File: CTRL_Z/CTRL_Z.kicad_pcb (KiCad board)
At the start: 2 copper layers, 25 x 20 mm, 6 parts, among them J1 BM04B-NSHSS-TBT_LF__SN_

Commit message: CTRL Z, R, PWR Cleanup! Changes Made:
CTRL PWR -> Added Ground Plane and Ground Vias. Moved it out of parent folder CTRL_R upto Root.
CTRL Z ->  Removed Unnecessary ZX pin. Added Ground Plane and Ground Vias.
CTRL R -> Cleaned up pin count, from 14 down to 10. Added Ground Plane and Ground Vias. Made some modifications to the board shape.
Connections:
- J1 pad 2: Row1_X -> unconnected-(J1-Pad2)
- J1 pad 3: Row1_ZX -> Net-(S1-COM_1)
- S1 pad 1: Row1_X -> Net-(S1-COM_1)
- S1 pad 2: Row1_X -> Net-(S1-COM_1)
- S2 pad 1: Row1_ZX -> Net-(S1-COM_1)
- S2 pad 2: Row1_ZX -> Net-(S1-COM_1)
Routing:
- net Net-(S1-COM_1): track 0.00 -> 33.5 mm, vias 0 -> 1
- net Row1_X: track 16.4 -> 0.00 mm, vias 1 -> 0
- net Row1_ZX: track 14.9 -> 0.00 mm, vias 1 -> 0
- net GND: vias 0 -> 4
- added copper zone on B.Cu, net GND
- added copper zone on F.Cu, net GND
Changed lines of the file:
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@@
 		(sheetname "/")
 		(sheetfile "CTRL_Z.kicad_sch")
+		(units
+			(unit
+				(name "A")
+				(pins)
+			)
+		)
 		(attr exclude_from_bom)
 		(duplicate_pad_numbers_are_jumpers no)
@@
 		(sheetname "/")
 		(sheetfile "CTRL_Z.kicad_sch")
+		(units
+			(unit
+				(name "A")
+				(pins "4" "2" "3" "1")
+			)
+		)
 		(attr smd)
 		(duplicate_pad_numbers_are_jumpers no)
@@
 			(size 1.3 1.55)
 			(layers "F.Cu" "F.Mask" "F.Paste")
-			(net "Row1_ZX")
+			(net "Net-(S1-COM_1)")
 			(pinfunction "COM_1_1")
 			(pintype "passive")
@@
 			(size 1.3 1.55)
 			(layers "F.Cu" "F.Mask" "F.Paste")
-			(net "Row1_ZX")
+			(net "Net-(S1-COM_1)")
 			(pinfunction "COM_2_2")
 			(pintype "passive")
@@
 		(sheetname "/")
 		(sheetfile "CTRL_Z.kicad_sch")
+		(units
+			(unit
+				(name "A")
+				(pins "4" "2" "3" "1")
+			)
+		)
 		(attr smd)
 		(duplicate_pad_numbers_are_jumpers no)
@@
 			(size 1.3 1.55)
 			(layers "F.Cu" "F.Mask" "F.Paste")
-			(net "Row1_X")
+			(net "Net-(S1-COM_1)")
 			(pinfunction "COM_1_1")
 			(pintype "passive")
@@
 			(size 1.3 1.55)
 			(layers "F.Cu" "F.Mask" "F.Paste")
-			(net "Row1_X")
+			(net "Net-(S1-COM_1)")
 			(pinfunction "COM_2_2")
 			(pintype "passive")
@@
 		(sheetname "/")
 		(sheetfile "CTRL_Z.kicad_sch")
+		(units
+			(unit
+				(name "A")
+				(pins)
+			)
+		)
 		(attr exclude_from_bom)
 		(duplicate_pad_numbers_are_jumpers no)
@@
 		(sheetname "/")
 		(sheetfile "CTRL_Z.kicad_sch")
+		(units
+			(unit
+				(name "A")
+				(pins)
+			)
+		)
 		(attr exclude_from_bom)
 		(duplicate_pad_numbers_are_jumpers no)
@@
 		(sheetname "/")
 		(sheetfile "CTRL_Z.kicad_sch")
+		(units
+			(unit
+				(name "A")
+				(pins "6" "5" "4" "3" "2" "1")
+			)
+		)
 		(attr smd)
 		(duplicate_pad_numbers_are_jumpers no)
@@
 			(size 0.6 1.7)
 			(layers "B.Cu" "B.Mask" "B.Paste")
-			(net "Row1_X")
+			(net "unconnected-(J1-Pad2)")
 			(pinfunction "2_2")
-			(pintype "passive")
+			(pintype "passive+no_connect")
 		)
 		(pad "3" smd rect
@@
 			(size 0.6 1.7)
 			(layers "B.Cu" "B.Mask" "B.Paste")
-			(net "Row1_ZX")
+			(net "Net-(S1-COM_1)")
 			(pinfunction "3_3")
 			(pintype "passive")
@@
 	)
 	(segment
-		(start 83.679 114.852)
-		(end 88.879 114.852)
-		(width 0.2)
-		(layer "B.Cu")
-		(net "GND")
+		(start 90.14 112.932)
+		(end 90.14 115.281)
+		(width 0.2)
+		(layer "F.Cu")
+		(net "Net-(S1-COM_1)")
+	)
+	(segment
+		(start 90.165 112.907)
+		(end 90.14 112.932)
+		(width 0.2)
+		(layer "F.Cu")
+		(net "Net-(S1-COM_1)")
+	)
+	(segment
+		(start 99.165 106.656)
+		(end 98.09 105.581)
+		(width 0.2)
+		(layer "F.Cu")
+		(net "Net-(S1-COM_1)")
 	)
 	(segment
@@
 		(width 0.2)
 		(layer "F.Cu")
-		(net "Row1_X")
-	)
-	(segment
-		(start 88.802 105.609)
-		(end 90.112 105.609)
-		(width 0.2)
-		(layer "F.Cu")
-		(net "Row1_X")
-	)
-	(via
-		(at 88.802 105.609)
-		(size 0.6)
-		(drill 0.3)
-		(layers "F.Cu" "B.Cu")
-		(net "Row1_X")
-	)
-	(segment
-		(start 85.779 108.632)
-		(end 88.802 105.609)
-		(width 0.2)
-		(layer "B.Cu")
-		(net "Row1_X")
-	)
-	(segment
-		(start 85.779 111.502)
-		(end 85.779 108.632)
-		(width 0.2)
-		(layer "B.Cu")
-		(net "Row1_X")
-	)
-	(segment
-		(start 90.14 112.932)
-		(end 90.14 115.281)
-		(width 0.2)
-		(layer "F.Cu")
-		(net "Row1_ZX")
-	)
-	(segment
-		(start 90.165 112.907)
-		(end 90.14 112.932)
-		(width 0.2)
-		(layer "F.Cu")
-		(net "Row1_ZX")
+		(net "Net-(S1-COM_1)")
+	)
+	(segment
+		(start 99.165 114.206)
+		(end 99.165 106.656)
+		(width 0.2)
+		(layer "F.Cu")
+		(net "Net-(S1-COM_1)")
 	)
 	(segment
@@
 		(width 0.2)
 		(layer "F.Cu")
-		(net "Row1_ZX")
+		(net "Net-(S1-COM_1)")
+	)
+	(segment
+		(start 98.09 115.281)
+		(end 99.165 114.206)
+		(width 0.2)
+		(layer "F.Cu")
+		(net "Net-(S1-COM_1)")
 	)
 	(via
@@
 		(drill 0.3)
 		(layers "F.Cu" "B.Cu")
-		(net "Row1_ZX")
+		(net "Net-(S1-COM_1)")
 	)
 	(segment
@@
 		(width 0.2)
 		(layer "B.Cu")
-		(net "Row1_ZX")
+		(net "Net-(S1-COM_1)")
 	)
 	(segment
@@
 		(width 0.2)
 		(layer "B.Cu")
-		(net "Row1_ZX")
+		(net "Net-(S1-COM_1)")
 	)
 	(segment
@@
 		(width 0.2)
 		(layer "B.Cu")
-		(net "Row1_ZX")
+		(net "Net-(S1-COM_1)")
 	)
 	(segment
@@
 		(net "ColB")
 	)
+	(via
+		(at 106.045 111.76)
+		(size 0.6)
+		(drill 0.3)
+		(layers "F.Cu" "B.Cu")
+		(free yes)
+		(net "GND")
+	)
+	(via
+		(at 100.33 98.425)
+		(size 0.6)
+		(drill 0.3)
+		(layers "F.Cu" "B.Cu")
+		(free yes)
+		(net "GND")
+	)
+	(via
+		(at 88.265 98.425)
+		(size 0.6)
+		(drill 0.3)
+		(layers "F.Cu" "B.Cu")
+		(free yes)
+		(net "GND")
+	)
+	(via
+		(at 106.045 104.14)
+		(size 0.6)
+		(drill 0.3)
+		(layers "F.Cu" "B.Cu")
+		(free yes)
+		(net "GND")
+	)
+	(segment
+		(start 83.679 114.852)
+		(end 88.879 114.852)
+		(width 0.2)
+		(layer "B.Cu")
+		(net "GND")
+	)
+	(zone
+		(net "GND")
+		(layer "F.Cu")
+		(name "Ground Plane")
+		(hatch edge 0.5)
+		(priority 1)
+		(connect_pads
+			(clearance 0.5)
+		)
+		(min_thickness 0.25)
+		(fill yes
+			(thermal_gap 0.5)
+			(thermal_bridge_width 0.5)
+			(island_removal_mode 0)
+		)
+		(polygon
+			(pts
+				(xy 81.95 97.488) (xy 106.949 97.481) (xy 106.947 117.476) (xy 81.951 117.488)
+			)
+		)
+	)
+	(zone
+		(net "GND")
+		(layer "B.Cu")
+		(name "Ground Plane")
+		(hatch edge 0.5)
+		(connect_pads
+			(clearance 0.5)
+		)
+		(min_thickness 0.25)
+		(fill yes
+			(thermal_gap 0.5)
+			(thermal_bridge_width 0.5)
+			(island_removal_mode 0)
+		)
+		(polygon
+			(pts
+				(xy 81.95 97.481) (xy 106.947 97.474) (xy 106.959 117.473) (xy 81.949 117.474)
+			)
+		)
+	)
 	(embedded_fonts no)

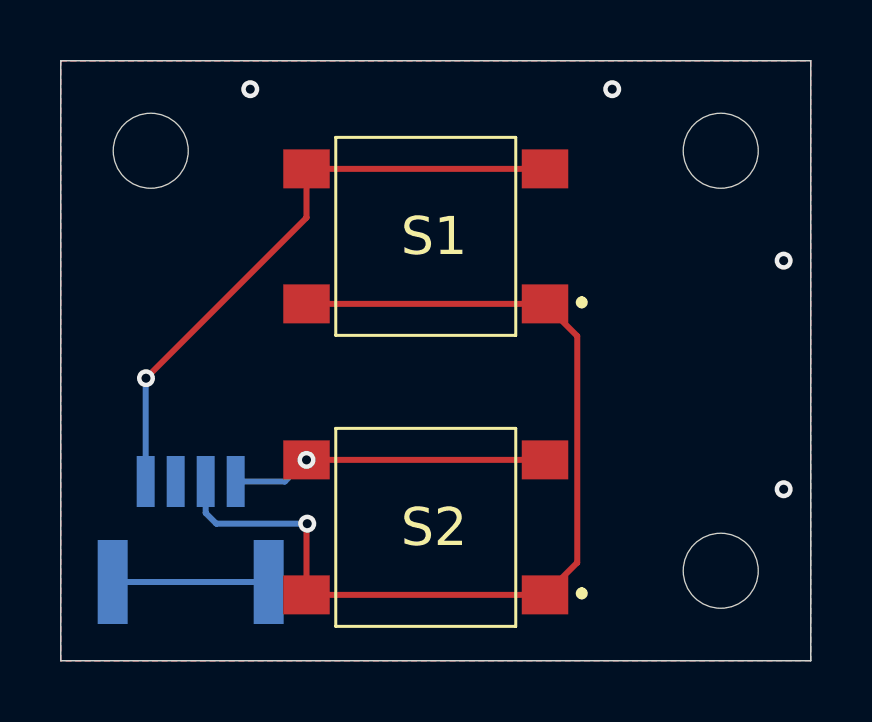
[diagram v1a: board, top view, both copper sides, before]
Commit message: Updated CTRL_Z to use 3 pin FPC and ESD Protection.
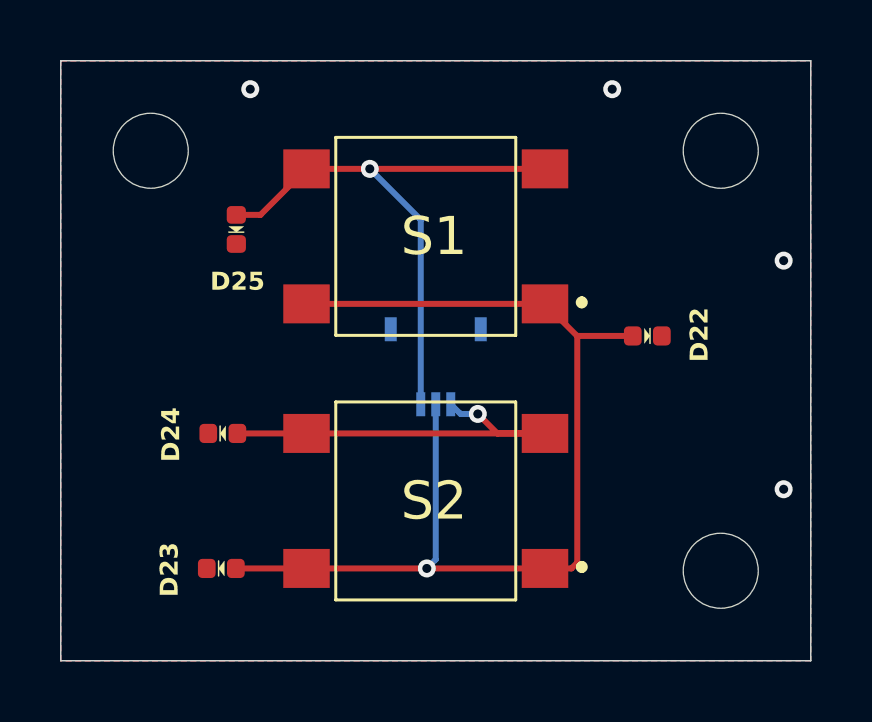
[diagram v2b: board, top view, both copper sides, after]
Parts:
- added D22: ESD5V0B03, A_HDJ_Library:D_0402_1005Metric, F.Cu at (101.5, 106.7)
- added D23: ESD5V0B03, A_HDJ_Library:D_0402_1005Metric, F.Cu at (87.3, 114.4)
- added D24: ESD5V0B03, A_HDJ_Library:D_0402_1005Metric, F.Cu at (87.3, 109.9)
- added D25: ESD5V0B03, A_HDJ_Library:D_0402_1005Metric, F.Cu at (87.8, 103.1)
- J1: value BM04B-NSHSS-TBT_LF__SN_ -> AYF530365TA; footprint BM04B-NSHSS-TBT:BM04BNSHSSTBTLFSN -> AYF530365TA:AYF530365T
- moved J1 10.3 mm to (94.4, 107.5), turned to 0 degrees
- moved S2 0.88 mm to (94.1, 112.2)
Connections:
- J1 pad 2: unconnected-(J1-Pad2) -> Net-(D22-A2)
- J1 pad 3: Net-(S1-COM_1) -> ColA
- J1 pad 4: ColA -> GND
- S1 pad 1: Net-(S1-COM_1) -> Net-(D22-A2)
- S1 pad 2: Net-(S1-COM_1) -> Net-(D22-A2)
- S2 pad 1: Net-(S1-COM_1) -> Net-(D22-A2)
- S2 pad 2: Net-(S1-COM_1) -> Net-(D22-A2)
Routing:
- net Net-(D22-A2): track 0.00 -> 35.9 mm, vias 0 -> 1
- net Net-(S1-COM_1): track 33.5 -> 0.00 mm, vias 1 -> 0
- net GND: track 5.20 -> 0.00 mm
- net ColA: track 10.6 -> 13.8 mm
- net ColB: track 20.6 -> 19.5 mm

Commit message: Updated CTRL_L to use 4 pin FPC (3 pin is hard to source!)
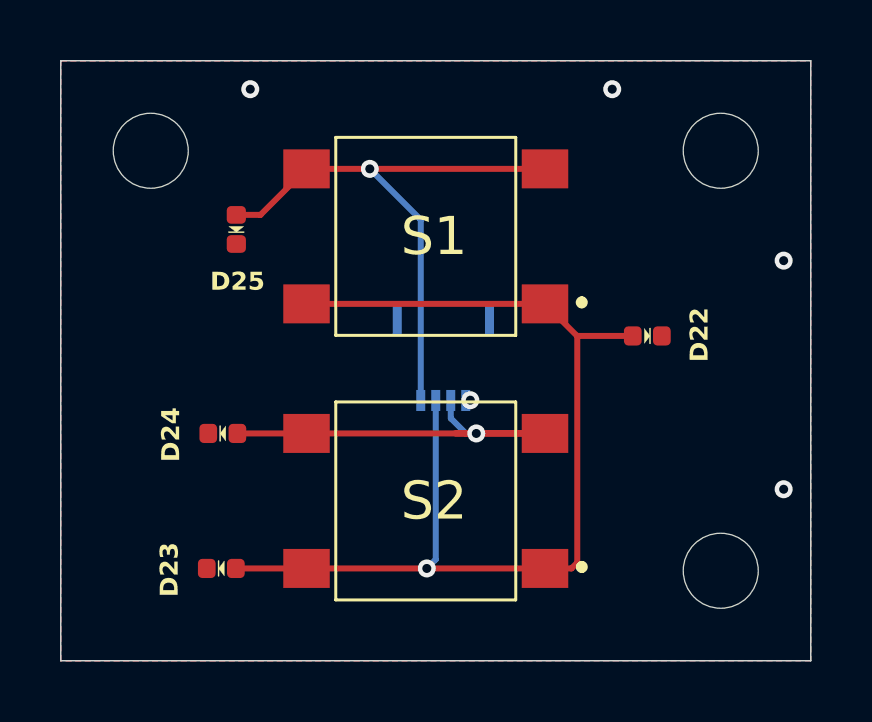
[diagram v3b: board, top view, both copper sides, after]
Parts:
- removed J1: AYF530365TA, AYF530365TA:AYF530365T
- added J2: 503480-0440, 503480-0440:5034800440, B.Cu at (94.7, 107.3)
- added kibuzzard-6A70E37C: G***, kibuzzard-6A70E37C, B.Cu at (91.7, 115.5)
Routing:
- net ColA: track 13.8 -> 14.6 mm
- net GND: track 0.00 -> 0.15 mm, vias 4 -> 5
